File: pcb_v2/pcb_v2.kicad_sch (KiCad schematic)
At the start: 31 parts

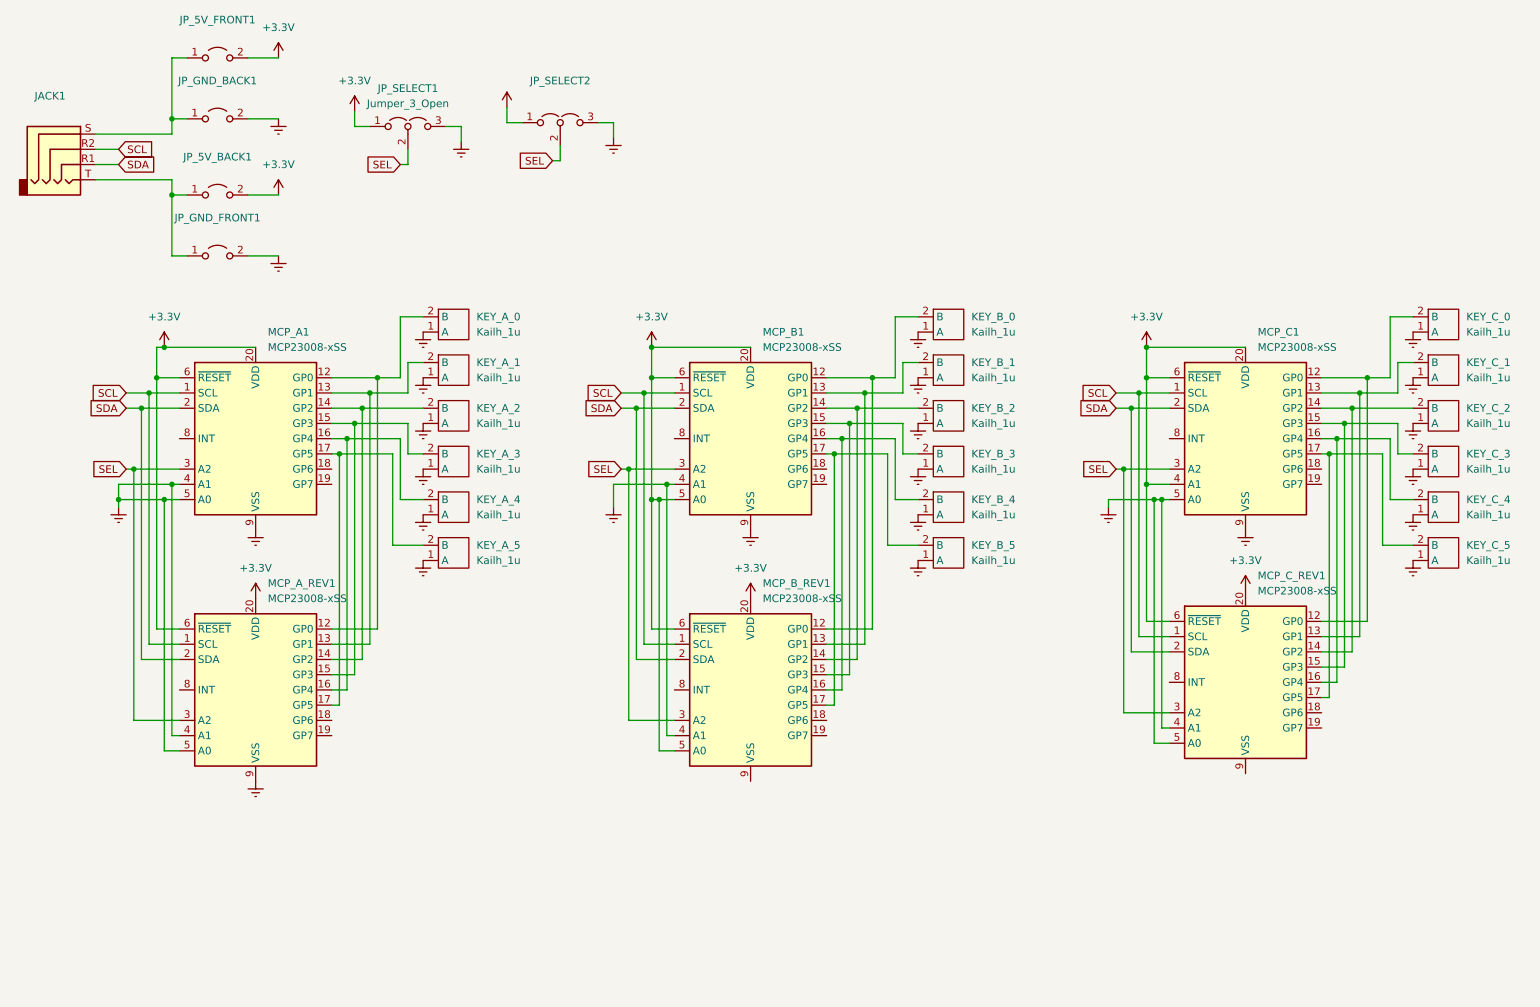
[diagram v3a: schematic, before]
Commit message: pcb v2 fixes + support for v2 in firmware
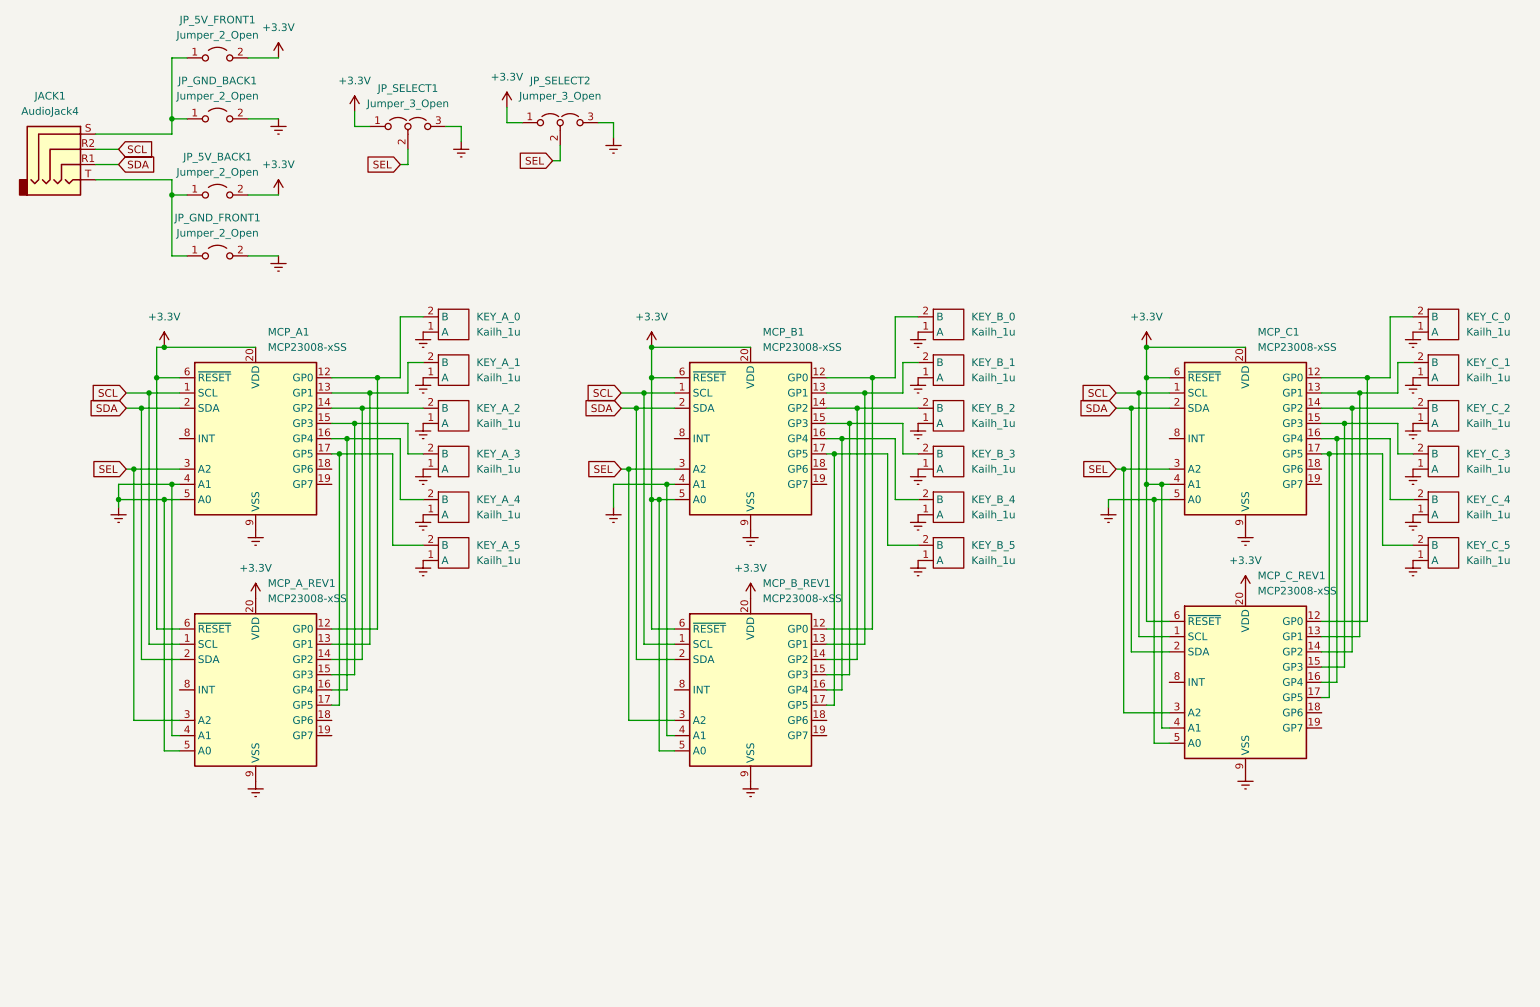
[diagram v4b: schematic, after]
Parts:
- JACK1: value (none) -> AudioJack4; footprint (none) -> PJ-320A:TRRS-PJ-320A-no-Fmask-reversible
- JP_5V_BACK1, JP_5V_FRONT1, JP_GND_BACK1, JP_GND_FRONT1: value (none) -> Jumper_2_Open; footprint (none) -> Jumper:SolderJumper-2_P1.3mm_Open_Pad1.0x1.5mm
- JP_SELECT2: value (none) -> Jumper_3_Open; footprint (none) -> Jumper:SolderJumper-3_P1.3mm_Open_Pad1.0x1.5mm
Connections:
- net +3V3: now also MCP_C_REV1.4 (A1)
- net Earth: now also MCP_B_REV1.9 (VSS), MCP_C_REV1.9 (VSS); no longer MCP_C_REV1.4 (A1)
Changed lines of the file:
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@@
   (junction (at 130.81 69.85) (diameter 0) (color 0 0 0 0)
   )
+  (junction (at 215.9 92.71) (diameter 0) (color 0 0 0 0)
+  )
   (junction (at 167.64 74.93) (diameter 0) (color 0 0 0 0)
   )
@@
   (junction (at 213.36 92.71) (diameter 0) (color 0 0 0 0)
   )
-  (junction (at 215.9 95.25) (diameter 0) (color 0 0 0 0)
-  )
   (junction (at 248.92 77.47) (diameter 0) (color 0 0 0 0)
   )
@@
     (stroke (width 0) (type default) (color 0 0 0 0))
   )
-  (wire (pts (xy 215.9 133.35) (xy 215.9 95.25))
+  (wire (pts (xy 215.9 92.71) (xy 215.9 133.35))
     (stroke (width 0) (type default) (color 0 0 0 0))
   )
@@
     (stroke (width 0) (type default) (color 0 0 0 0))
   )
+  (wire (pts (xy 214.63 95.25) (xy 217.17 95.25))
+    (stroke (width 0) (type default) (color 0 0 0 0))
+  )
   (wire (pts (xy 160.02 80.01) (xy 165.1 80.01))
     (stroke (width 0) (type default) (color 0 0 0 0))
   )
+  (wire (pts (xy 215.9 92.71) (xy 213.36 92.71))
+    (stroke (width 0) (type default) (color 0 0 0 0))
+  )
   (wire (pts (xy 41.91 95.25) (xy 41.91 96.52))
     (stroke (width 0) (type default) (color 0 0 0 0))
@@
     (stroke (width 0) (type default) (color 0 0 0 0))
   )
-  (wire (pts (xy 215.9 95.25) (xy 217.17 95.25))
-    (stroke (width 0) (type default) (color 0 0 0 0))
-  )
   (wire (pts (xy 246.38 82.55) (xy 255.27 82.55))
     (stroke (width 0) (type default) (color 0 0 0 0))
@@
     (stroke (width 0) (type default) (color 0 0 0 0))
   )
-  (wire (pts (xy 217.17 92.71) (xy 213.36 92.71))
+  (wire (pts (xy 217.17 92.71) (xy 215.9 92.71))
     (stroke (width 0) (type default) (color 0 0 0 0))
   )
@@
   )
   (wire (pts (xy 90.17 39.37) (xy 90.17 36.83))
-    (stroke (width 0) (type default) (color 0 0 0 0))
-  )
-  (wire (pts (xy 214.63 95.25) (xy 215.9 95.25))
     (stroke (width 0) (type default) (color 0 0 0 0))
   )
@@
     (in_bom yes) (on_board yes) (fields_autoplaced)
     (property "Reference" "JP_GND_FRONT1" (id 0) (at 58.42 48.26 0))
-    (property "Value" "" (id 1) (at 58.42 50.8 0))
-    (property "Footprint" "" (id 2) (at 58.42 54.61 0)
+    (property "Value" "Jumper_2_Open" (id 1) (at 58.42 50.8 0))
+    (property "Footprint" "Jumper:SolderJumper-2_P1.3mm_Open_Pad1.0x1.5mm" (id 2) (at 58.42 54.61 0)
       (effects (font (size 1.27 1.27)) hide)
     )
@@
     (pin "2")
   )
+  (symbol (lib_id "power:Earth") (at 147.32 142.24 0) (unit 1)
+    (in_bom yes) (on_board yes) (fields_autoplaced)
+    (property "Reference" "#PWR?" (id 0) (at 147.32 148.59 0)
+      (effects (font (size 1.27 1.27)) hide)
+    )
+    (property "Value" "Earth" (id 1) (at 147.32 146.05 0)
+      (effects (font (size 1.27 1.27)) hide)
+    )
+    (property "Footprint" "" (id 2) (at 147.32 142.24 0)
+      (effects (font (size 1.27 1.27)) hide)
+    )
+    (property "Datasheet" "~" (id 3) (at 147.32 142.24 0)
+      (effects (font (size 1.27 1.27)) hide)
+    )
+    (pin "1")
+  )
   (symbol (lib_id "projectLibrary:Kailh_1u") (at 92.71 96.52 0) (unit 1)
     (in_bom yes) (on_board yes) (fields_autoplaced)
@@
     (in_bom yes) (on_board yes) (fields_autoplaced)
     (property "Reference" "JP_SELECT2" (id 0) (at 115.57 25.4 0))
-    (property "Value" "" (id 1) (at 115.57 27.94 0))
-    (property "Footprint" "" (id 2) (at 115.57 32.385 0)
+    (property "Value" "Jumper_3_Open" (id 1) (at 115.57 27.94 0))
+    (property "Footprint" "Jumper:SolderJumper-3_P1.3mm_Open_Pad1.0x1.5mm" (id 2) (at 115.57 32.385 0)
       (effects (font (size 1.27 1.27)) hide)
     )
@@
     (pin "1")
   )
+  (symbol (lib_id "power:Earth") (at 229.87 140.97 0) (unit 1)
+    (in_bom yes) (on_board yes) (fields_autoplaced)
+    (property "Reference" "#PWR?" (id 0) (at 229.87 147.32 0)
+      (effects (font (size 1.27 1.27)) hide)
+    )
+    (property "Value" "Earth" (id 1) (at 229.87 144.78 0)
+      (effects (font (size 1.27 1.27)) hide)
+    )
+    (property "Footprint" "" (id 2) (at 229.87 140.97 0)
+      (effects (font (size 1.27 1.27)) hide)
+    )
+    (property "Datasheet" "~" (id 3) (at 229.87 140.97 0)
+      (effects (font (size 1.27 1.27)) hide)
+    )
+    (pin "1")
+  )
   (symbol (lib_id "Jumper:Jumper_2_Open") (at 58.42 31.75 0) (unit 1)
     (in_bom yes) (on_board yes) (fields_autoplaced)
     (property "Reference" "JP_GND_BACK1" (id 0) (at 58.42 25.4 0))
-    (property "Value" "" (id 1) (at 58.42 27.94 0))
-    (property "Footprint" "" (id 2) (at 58.42 31.75 0)
+    (property "Value" "Jumper_2_Open" (id 1) (at 58.42 27.94 0))
+    (property "Footprint" "Jumper:SolderJumper-2_P1.3mm_Open_Pad1.0x1.5mm" (id 2) (at 58.42 31.75 0)
       (effects (font (size 1.27 1.27)) hide)
     )
@@
       (effects (font (size 1.27 1.27)) hide)
     )
-    (property "Value" "" (id 1) (at 106.68 24.765 0))
+    (property "Value" "+3.3V" (id 1) (at 106.68 24.765 0))
     (property "Footprint" "" (id 2) (at 106.68 29.845 0)
       (effects (font (size 1.27 1.27)) hide)
@@
     (in_bom yes) (on_board yes) (fields_autoplaced)
     (property "Reference" "JP_5V_FRONT1" (id 0) (at 58.42 15.24 0))
-    (property "Value" "" (id 1) (at 58.42 17.78 0))
-    (property "Footprint" "" (id 2) (at 58.42 21.59 0)
+    (property "Value" "Jumper_2_Open" (id 1) (at 58.42 17.78 0))
+    (property "Footprint" "Jumper:SolderJumper-2_P1.3mm_Open_Pad1.0x1.5mm" (id 2) (at 58.42 21.59 0)
       (effects (font (size 1.27 1.27)) hide)
     )
@@
     (in_bom yes) (on_board yes) (fields_autoplaced)
     (property "Reference" "JACK1" (id 0) (at 30.48 27.94 0))
-    (property "Value" "" (id 1) (at 30.48 30.48 0))
-    (property "Footprint" "" (id 2) (at 33.02 36.83 0)
+    (property "Value" "AudioJack4" (id 1) (at 30.48 30.48 0))
+    (property "Footprint" "PJ-320A:TRRS-PJ-320A-no-Fmask-reversible" (id 2) (at 33.02 36.83 0)
       (effects (font (size 1.27 1.27)) hide)
     )
@@
     (in_bom yes) (on_board yes) (fields_autoplaced)
     (property "Reference" "JP_5V_BACK1" (id 0) (at 58.42 38.1 0))
-    (property "Value" "" (id 1) (at 58.42 40.64 0))
-    (property "Footprint" "" (id 2) (at 58.42 44.45 0)
+    (property "Value" "Jumper_2_Open" (id 1) (at 58.42 40.64 0))
+    (property "Footprint" "Jumper:SolderJumper-2_P1.3mm_Open_Pad1.0x1.5mm" (id 2) (at 58.42 44.45 0)
       (effects (font (size 1.27 1.27)) hide)
     )
@@
       (reference "#PWR0139") (unit 1) (value "+3.3V") (footprint "")
     )
+    (path "/90d33e02-fb2f-4dc7-ad2e-67e9cae04ef5"
+      (reference "#PWR?") (unit 1) (value "Earth") (footprint "")
+    )
+    (path "/a9ab623c-bc91-4cfd-9357-bc71cc66025d"
+      (reference "#PWR?") (unit 1) (value "Earth") (footprint "")
+    )
     (path "/d1dcaffa-ed05-40d4-950f-95ceb666e2c3"
